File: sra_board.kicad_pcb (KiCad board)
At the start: 2 copper layers, 90 x 70.1 mm, 163 parts, among them J1 Barrel_Jack, J10 B2B-XH-A_LF__SN_, J11 Conn_01x03_Pin, J12 Conn_01x03_Pin, J13 Conn_01x03_Pin, J14 MPU0650, J15 Conn_01x03_Pin, J16 LSA, J17 OLED, J18 B2B-XH-A_LF__SN_, J2 Conn_01x03_Pin, J3 USB_C_Receptacle_USB2.0_16P, J4 Conn_01x14_Pin, J5 Conn_01x03_Pin, J6 Conn_01x08_Pin, J7 Conn_01x03_Pin, J8 Conn_01x14_Pin, J9 B2B-XH-A_LF__SN_, Q1 DMN3016lss, Q2 SI4435FDY, Q3 SS8050, Q4 SS8050, Q7 ZXMP4A16GTA, SW1 SW_0, SW2 SW_EN, SW3 SW_Wuerth_450301014042, SW4 SW_Wuerth_450301014042, U1 ESP32-WROOM-32E, U2 CN3303, U3 CH340C, U4 TB6612FNG H-bridge Motor Driv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, U5 AMS1117-3.3, U6 MAX7219CWG_T, U7 TPS54302

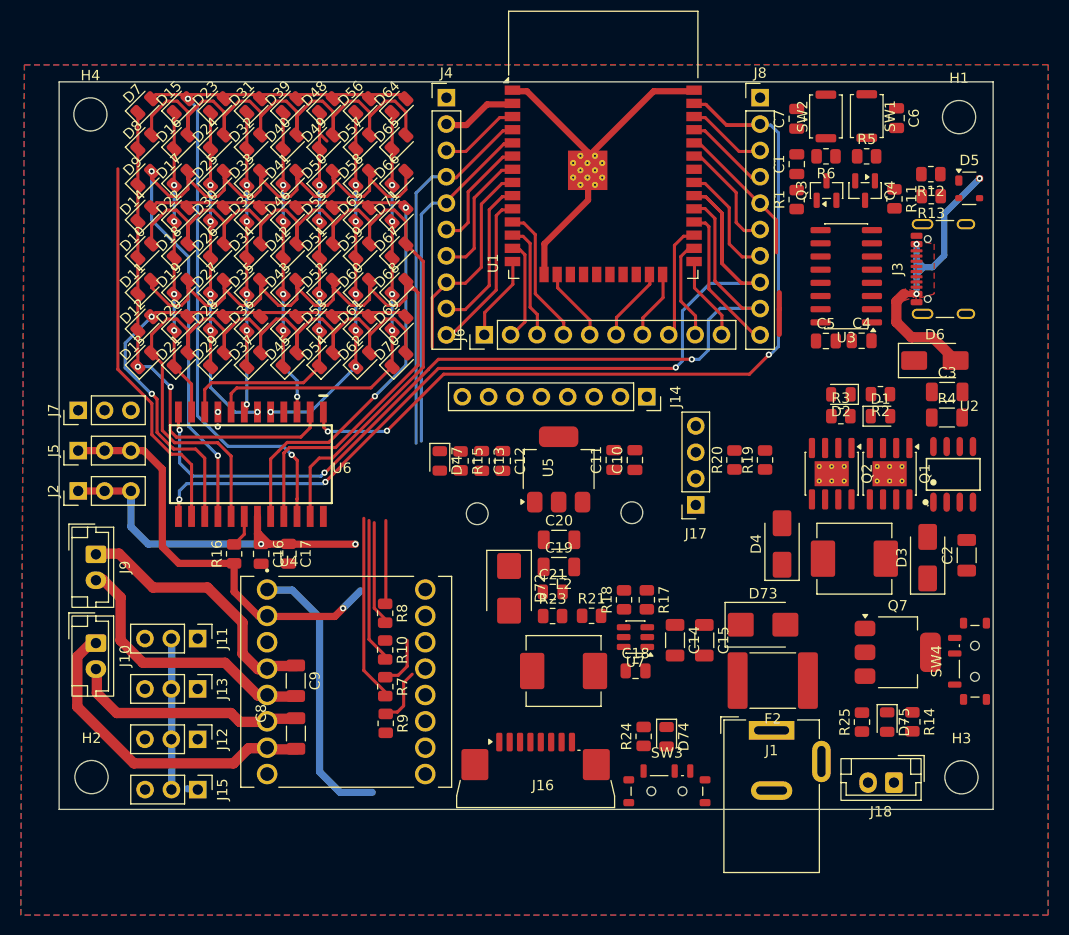
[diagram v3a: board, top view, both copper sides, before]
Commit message: Adding new fully routed PCB without CN3303 and controlling the EN pin of TPS with switch rather than actual power line
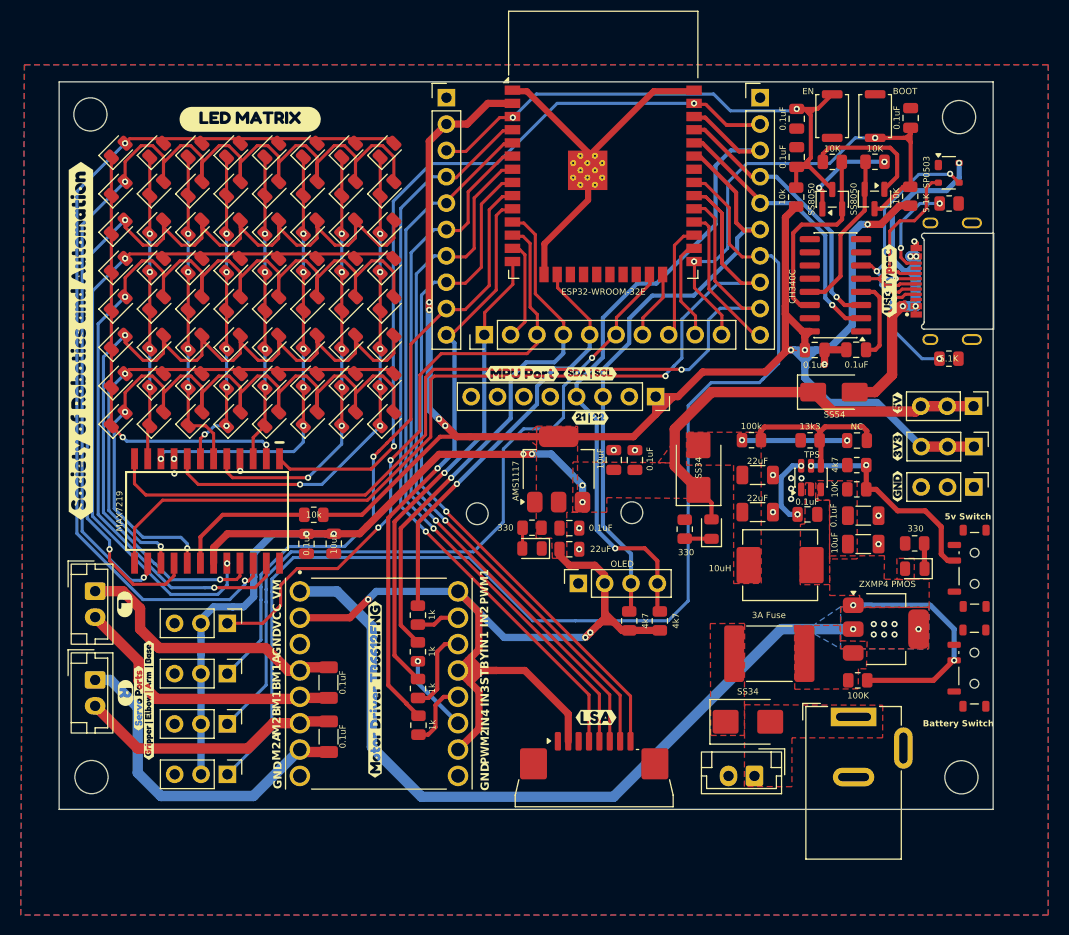
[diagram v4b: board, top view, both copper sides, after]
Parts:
- removed C2, C3: 22uF, Capacitor_SMD:C_1206_3216Metric
- removed D1, D2: LED, LED_SMD:LED_0805_2012Metric
- removed D3, D4: SS54, Diode_SMD:D_SMA
- removed L1: 6.8uH, Inductor_SMD:L_Sunlord_MWSA0603S
- removed Q1: DMN3016lss, Package_SO:SOIC-8-1EP_3.9x4.9mm_P1.27mm_EP2.41x3.3mm_ThermalVias
- removed Q2: SI4435FDY, Package_SO:SOIC-8-1EP_3.9x4.9mm_P1.27mm_EP2.41x3.3mm_ThermalVias
- removed R2, R3: 1k, Resistor_SMD:R_0805_2012Metric
- removed R4: 40m, Resistor_SMD:R_1206_3216Metric
- removed U2: CN3303, easyeda2kicad:SOP-8_L4.9-W3.9-P1.27-LS6.0-BL
- added G***: LOGO, logos:espressif_logo, B.Cu at (93.6, 61.4)
- added G***: LOGO, Logos:Lions_logo, B.Cu at (90.3, 108.6)
- added G***: LOGO, logos:sra_skull_big, B.Cu at (89.1, 91.6)
- added G***: LOGO, Logos:sra_logo_big, B.Cu at (118.8, 63.0)
- added kibuzzard-658F2C3C: G***, kibuzzard-658F2C3C, F.Cu at (92.8, 115.5)
- added kibuzzard-668D4F81: G***, kibuzzard-668D4F81, F.Cu at (85.7, 82.4)
- added kibuzzard-668FE423: G***, kibuzzard-668FE423, F.Cu at (121.1, 73.4)
- added kibuzzard-66914CE9: G***, kibuzzard-66914CE9, B.Cu at (93.6, 69.5)
- added kibuzzard-66921043: G***, kibuzzard-66921043, B.Cu at (93.8, 67.5)
- added kibuzzard-66923428: G***, kibuzzard-66923428, F.Cu at (71.5, 112.8)
- added kibuzzard-66CD8CDE: G***, kibuzzard-66CD8CDE, F.Cu at (49.7, 113.9)
- added kibuzzard-66CD901B: G***, kibuzzard-66CD901B, F.Cu at (48.7, 113.7)
- added kibuzzard-675FDA6A: G***, kibuzzard-675FDA6A, F.Cu at (43.2, 79.2)
- added kibuzzard-675FE5A8: G***, kibuzzard-675FE5A8, F.Cu at (92.3, 86.7)
- added kibuzzard-675FE5B2: G***, kibuzzard-675FE5B2, F.Cu at (92.3, 82.4)
- added kibuzzard-67704CCE: G***, kibuzzard-67704CCE, F.Cu at (121.9, 93.3)
- added kibuzzard-67704CDF: G***, kibuzzard-67704CDF, F.Cu at (121.9, 89.4)
- added kibuzzard-67704CF4: G***, kibuzzard-67704CF4, F.Cu at (121.9, 85.2)
- added kibuzzard-6774F4AA: G***, kibuzzard-6774F4AA, F.Cu at (47.5, 113.2)
- added kibuzzard-6774F4AE: G***, kibuzzard-6774F4AE, F.Cu at (47.4, 104.6)
- added kibuzzard-68E7F907: G***, kibuzzard-68E7F907, F.Cu at (59.5, 57.9)
- F2: value 3A -> 3A Fuse
- J3: footprint Connector_USB:USB_C_Receptacle_GCT_USB4105-xx-A_16P_TopMnt_Horizontal -> footprints:AMPHENOL_GSB1C4621DS1HR
- Q7: value ZXMP4A16GTA -> ZXMP4 PMOS
- SW1: value SW_0 -> BOOT
- SW2: value SW_EN -> EN
- U5: value AMS1117-3.3 -> AMS1117
- U6: value MAX7219CWG_T -> MAX7219
- U7: value TPS54302 -> TPS
- moved J2 86.7 mm to (129.2, 85.5), turned to -90 degrees
- moved J7 86.6 mm to (129.2, 93.3), turned to -90 degrees
- moved J5 86.3 mm to (129.2, 89.4), turned to -90 degrees
- moved SW3 36.6 mm to (129.3, 101.2), turned to 90 degrees
- moved C21 32.8 mm to (118.0, 88.8)
- moved R21 27.0 mm to (113.5, 88.8), turned to 180 degrees
- moved R18 25.9 mm to (118.0, 91.2), turned to 0 degrees
- moved R23 25.6 mm to (107.8, 88.8)
- moved L2 23.2 mm to (110.6, 100.8)
- moved R17 22.9 mm to (118.0, 93.5), turned to 180 degrees
- moved U7 22.9 mm to (113.5, 92.4), turned to 90 degrees
- moved C18 22.4 mm to (113.2, 96.0)
- moved D72 21.7 mm to (102.7, 91.4), turned to 90 degrees
- moved D74 20.5 mm to (104.0, 97.4), turned to 90 degrees
- moved C14 20.4 mm to (118.6, 98.8), turned to 0 degrees
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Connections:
- J18 pad 1: GND -> +BATT
- J18 pad 2: +BATT -> GND
- R17 pad 1: /EN -> /EN_TPS
- R18 pad 2: /EN -> /EN_TPS
- SW3 pad 1: /EN -> /EN_TPS
- U7 pad 5: /EN -> /EN_TPS
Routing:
- net /3V3: track 52.0 -> 271.9 mm, vias 1 -> 10
- net /19: track 11.4 -> 117.2 mm
- net /5V_P: track 51.0 -> 120.3 mm, vias 2 -> 6
- net /15: track 7.14 -> 72.1 mm, vias 0 -> 1
- net /34: track 11.0 -> 70.4 mm, vias 0 -> 1
- net /22: track 7.72 -> 66.9 mm, vias 0 -> 1
- net /35: track 12.7 -> 69.5 mm, vias 0 -> 1
- net /27: track 11.1 -> 60.5 mm, vias 0 -> 2
- net /12V: track 26.8 -> 75.0 mm, vias 0 -> 8
- net /EN: track 7.72 -> 55.3 mm, vias 0 -> 2
- net /32: track 20.7 -> 68.2 mm, vias 0 -> 1
- net /21: track 11.0 -> 58.2 mm
- net /33: track 15.2 -> 62.2 mm, vias 0 -> 1
- net /0: track 8.15 -> 49.3 mm, vias 0 -> 2
- net /26: track 13.5 -> 51.9 mm, vias 0 -> 1
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- added copper zone on F.Cu, net +BATT
- added copper zone on B.Cu, net /12V
- added copper zone on F.Cu, net /12V
- added copper zone on F.Cu, net /3V3
- added copper zone on F.Cu, net /5V_P
- added copper zone on F.Cu, net Net-(D72-A)
- added copper zone on F.Cu, net Net-(D73-K)
- added copper zone on F.Cu, net Net-(Q7-S)
- added copper zone on F.Cu, net Net-(U7-SW)
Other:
- board text added: "5v Switch"
- board text added: "Battery Switch"
- board text added: "GND"
- board text added: "IN1"
- board text added: "IN2"
- board text added: "IN3"
- board text added: "IN4"
- board text added: "M1A"
- board text added: "M1B"
- board text added: "M2A"
- board text added: "M2B"
- board text added: "PWM1"
- board text added: "PWM2"
- board text added: "STBY"
- board text added: "VCC"
- board text added: "VM"
- board text added: "sravjti.in"

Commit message: Making minor fixes in pcb
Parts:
- added G***: LOGO, logos:sra_skull_big, F.Cu at (74.0, 95.2)
- added kibuzzard-675FE5A8: G***, kibuzzard-675FE5A8, F.Cu at (97.6, 100.2)
- added kibuzzard-6A8B3292: G***, kibuzzard-6A8B3292, F.Cu at (97.6, 98.5)
- D6: value SS54 -> SS14
- F2: value 3A Fuse -> 3A
- H1, H2, H3, H4: footprint MountingHole:MountingHole_3.2mm_M3_DIN965 -> MountingHole:MountingHole_3.2mm_M3_DIN965_Pad
- Q7: value ZXMP4 PMOS -> ZXMP4A16GTA
- SW1: value BOOT -> SW_0
- SW2: value EN -> SW_EN
- U5: value AMS1117 -> AMS1117-3.3
- U6: value MAX7219 -> MAX7219CWG_T
- U7: value TPS -> TPS54302
- moved D74 2.63 mm to (101.3, 97.4), turned to -90 degrees
- moved R24 2.53 mm to (103.9, 97.4), turned to 90 degrees
- moved D75 2.53 mm to (123.5, 98.7), turned to 0 degrees
- moved R25 2.33 mm to (123.6, 101.1), turned to 180 degrees
- moved H1 0.39 mm to (128.0, 57.3)
- moved D73 0.18 mm to (107.3, 115.9)
- moved F2 0.15 mm to (109.4, 109.4)
- moved H4 0.10 mm to (44.1, 57.3)
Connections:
- D74 pad 1: Net-(D74-K) -> GND
- D74 pad 2: /5V_P -> Net-(D74-A)
- D75 pad 1: Net-(D75-K) -> GND
- D75 pad 2: /12V -> Net-(D75-A)
- R24 pad 1: GND -> Net-(D74-A)
- R24 pad 2: Net-(D74-K) -> /5V_P
- R25 pad 1: GND -> Net-(D75-A)
- R25 pad 2: Net-(D75-K) -> /12V
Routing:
- net Net-(D74-K): track 2.59 -> 0.00 mm
- net Net-(D74-A): track 0.00 -> 2.59 mm
- net Net-(D75-K): track 2.36 -> 0.00 mm
- net Net-(D75-A): track 0.00 -> 2.36 mm
- net Net-(Q7-G): track 24.7 -> 26.6 mm
- net Net-(U7-FB): track 16.7 -> 17.4 mm
- net GND: vias 17 -> 18
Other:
- board text added: "12v"
- board text added: "3v3"
- board text added: "5v"

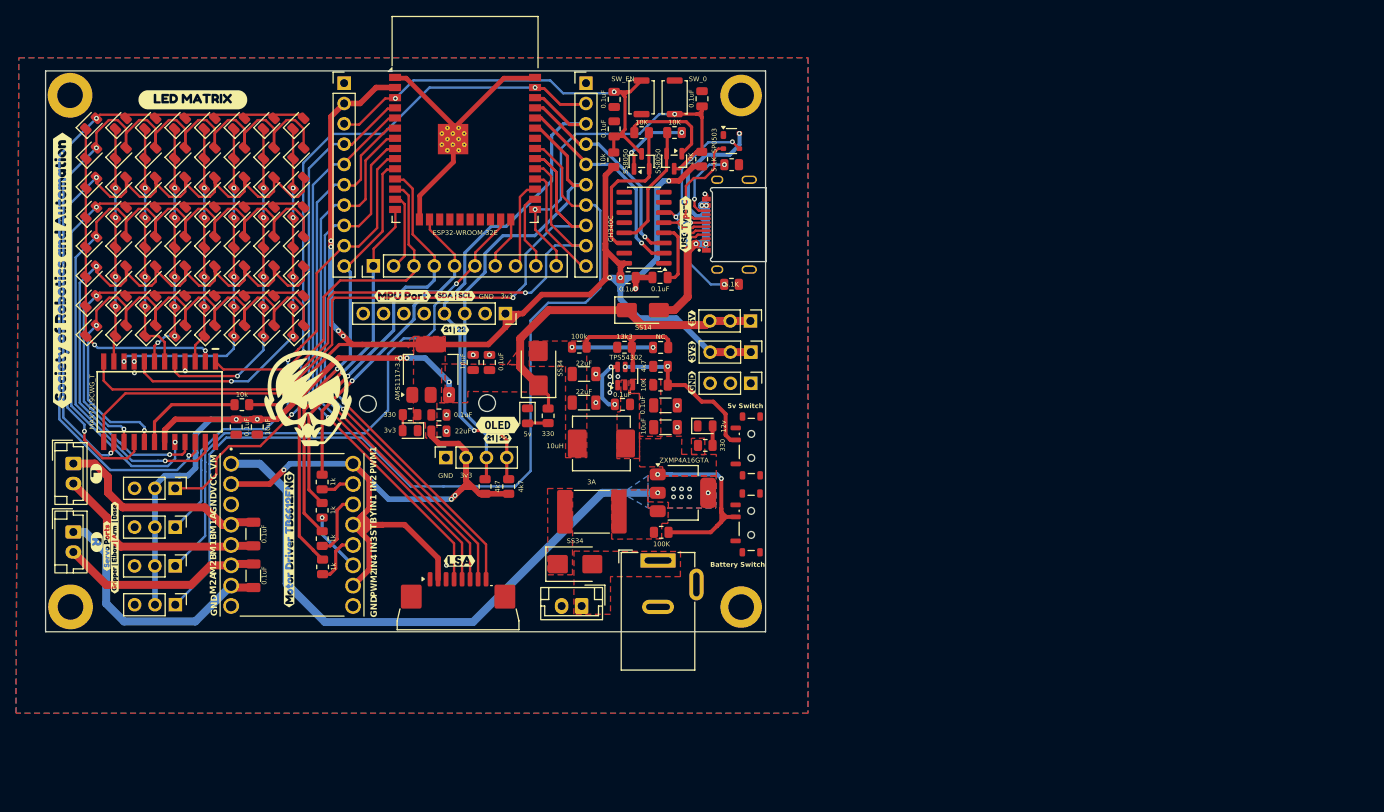
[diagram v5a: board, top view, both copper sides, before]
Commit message: Adding LSA and centering the LSA connector on SRA board
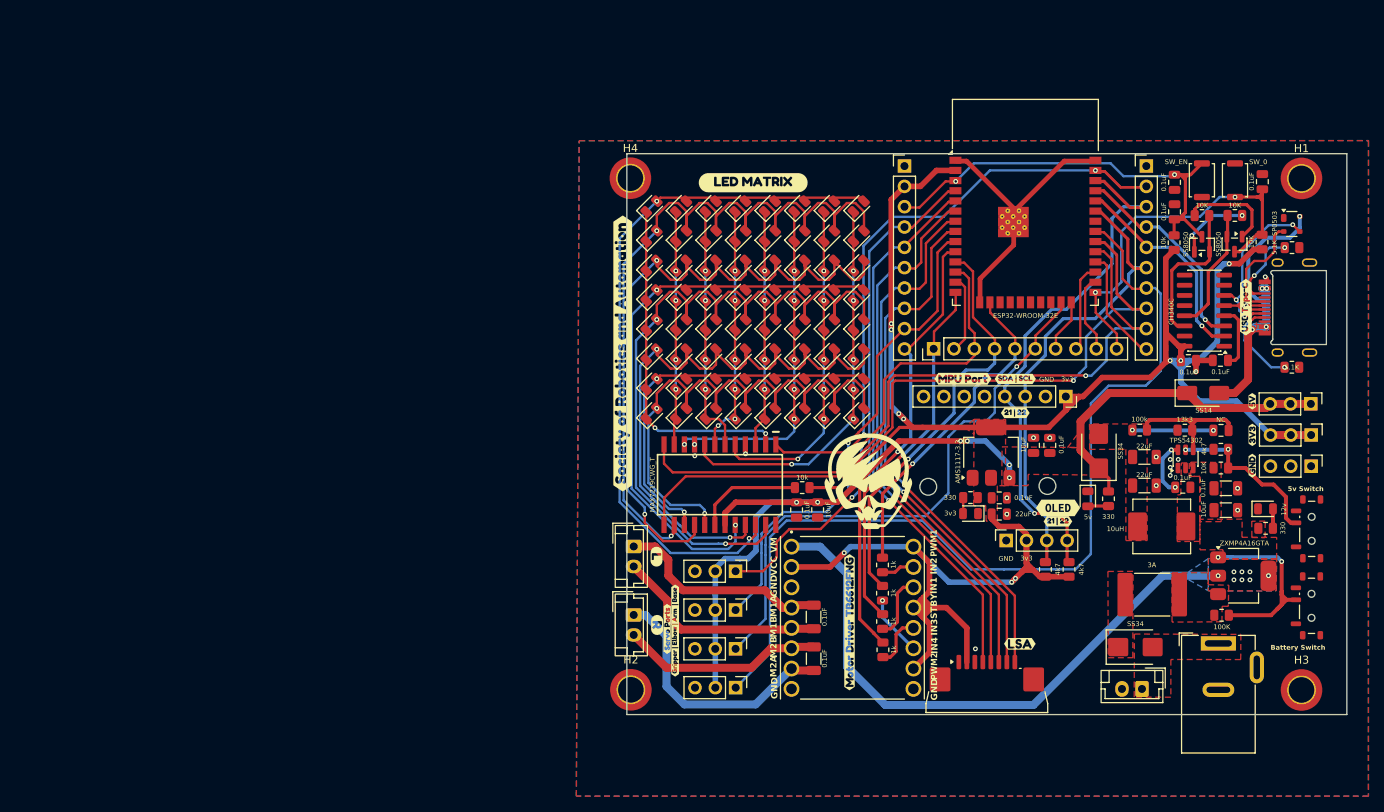
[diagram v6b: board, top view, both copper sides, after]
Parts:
- H1, H2, H3, H4: footprint MountingHole:MountingHole_3.2mm_M3_DIN965_Pad -> MountingHole:MountingHole_3.2mm_M3_DIN965_Pad_TopOnly
- moved C11 70.8 mm to (164.6, 101.1)
- moved J3 70.8 mm to (199.1, 83.9)
- moved R20 70.8 mm to (169.0, 116.6)
- moved R23 70.8 mm to (177.9, 99.2)
- moved SW3 70.8 mm to (199.4, 111.5)
- moved kibuzzard-68E7F907 70.8 mm to (129.5, 68.2)
- moved C18 70.8 mm to (183.2, 106.3)
- moved C21 70.8 mm to (188.0, 99.2)
- moved C4 70.8 mm to (187.9, 90.5)
- moved C5 70.8 mm to (183.9, 90.5)
- moved C6 70.8 mm to (193.2, 68.1)
- moved C8 70.8 mm to (137.1, 127.7)
- moved D10 70.8 mm to (116.8, 86.0)
- moved D11 70.8 mm to (116.8, 89.7)
- moved D12 70.8 mm to (116.8, 93.4)
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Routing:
- net /3V3: track 271.9 -> 267.5 mm
- net /39: track 70.6 -> 69.0 mm
- net /36: track 72.8 -> 71.1 mm
- net /32: track 68.2 -> 66.5 mm
- net /35: track 69.5 -> 67.8 mm
- net /34: track 70.4 -> 68.7 mm
- net /D+: track 22.2 -> 21.6 mm
